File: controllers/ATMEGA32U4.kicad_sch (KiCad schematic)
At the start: 12 parts, among them J1 USB_C2, U401 ATmega32U4-A, Y401 16MHz

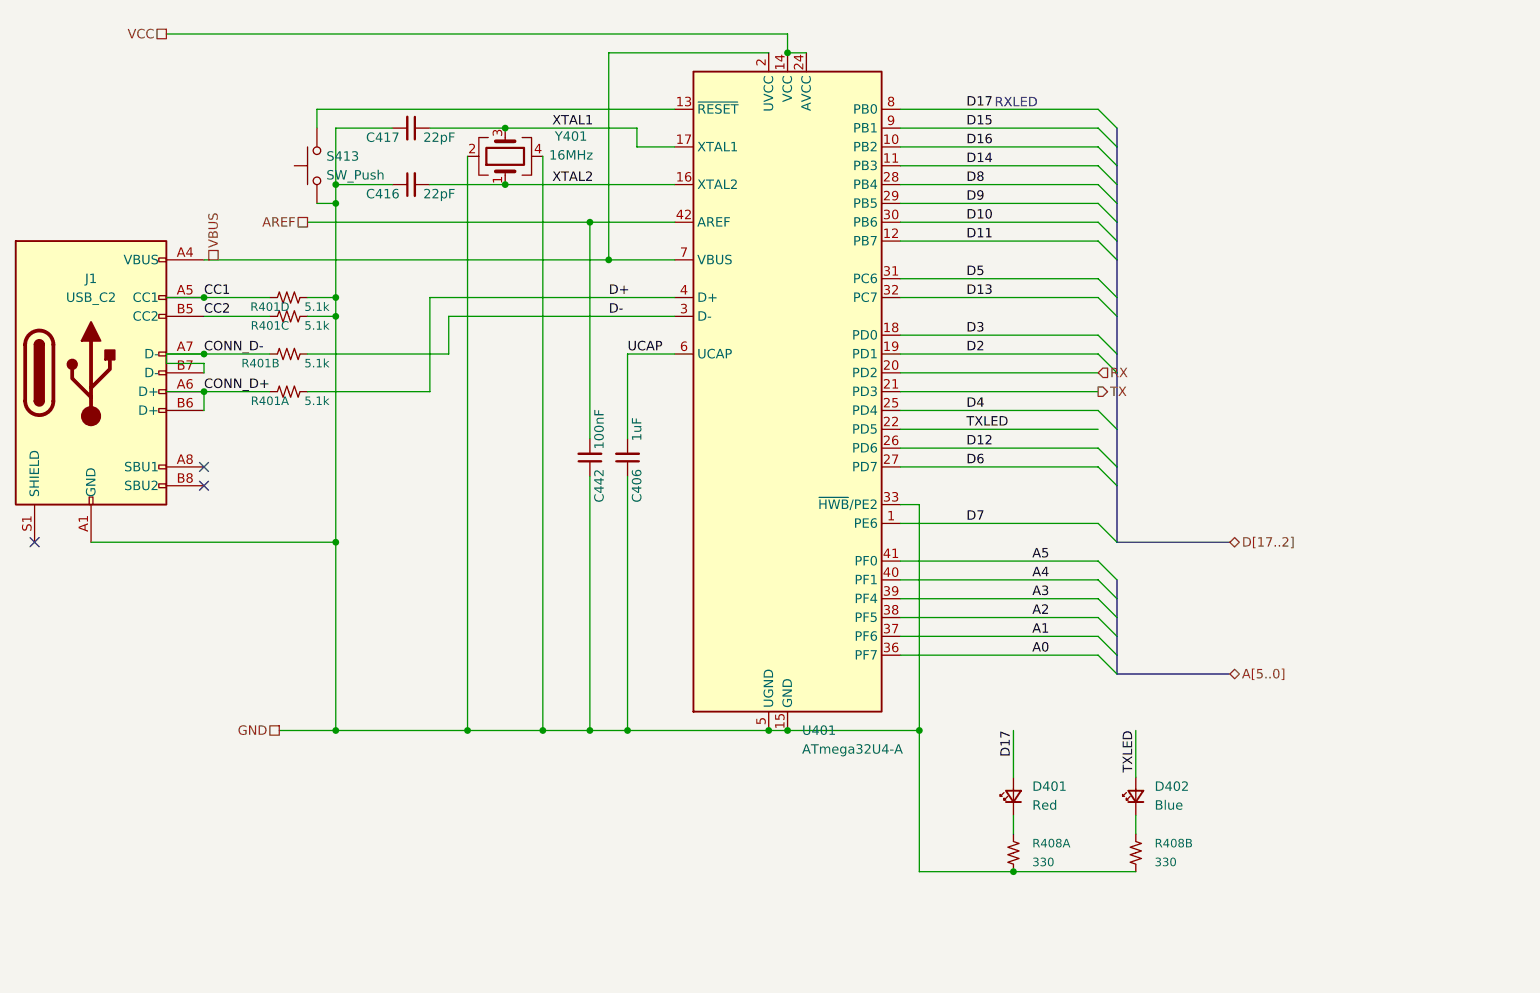
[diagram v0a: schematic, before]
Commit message: Use the separate hand sheets
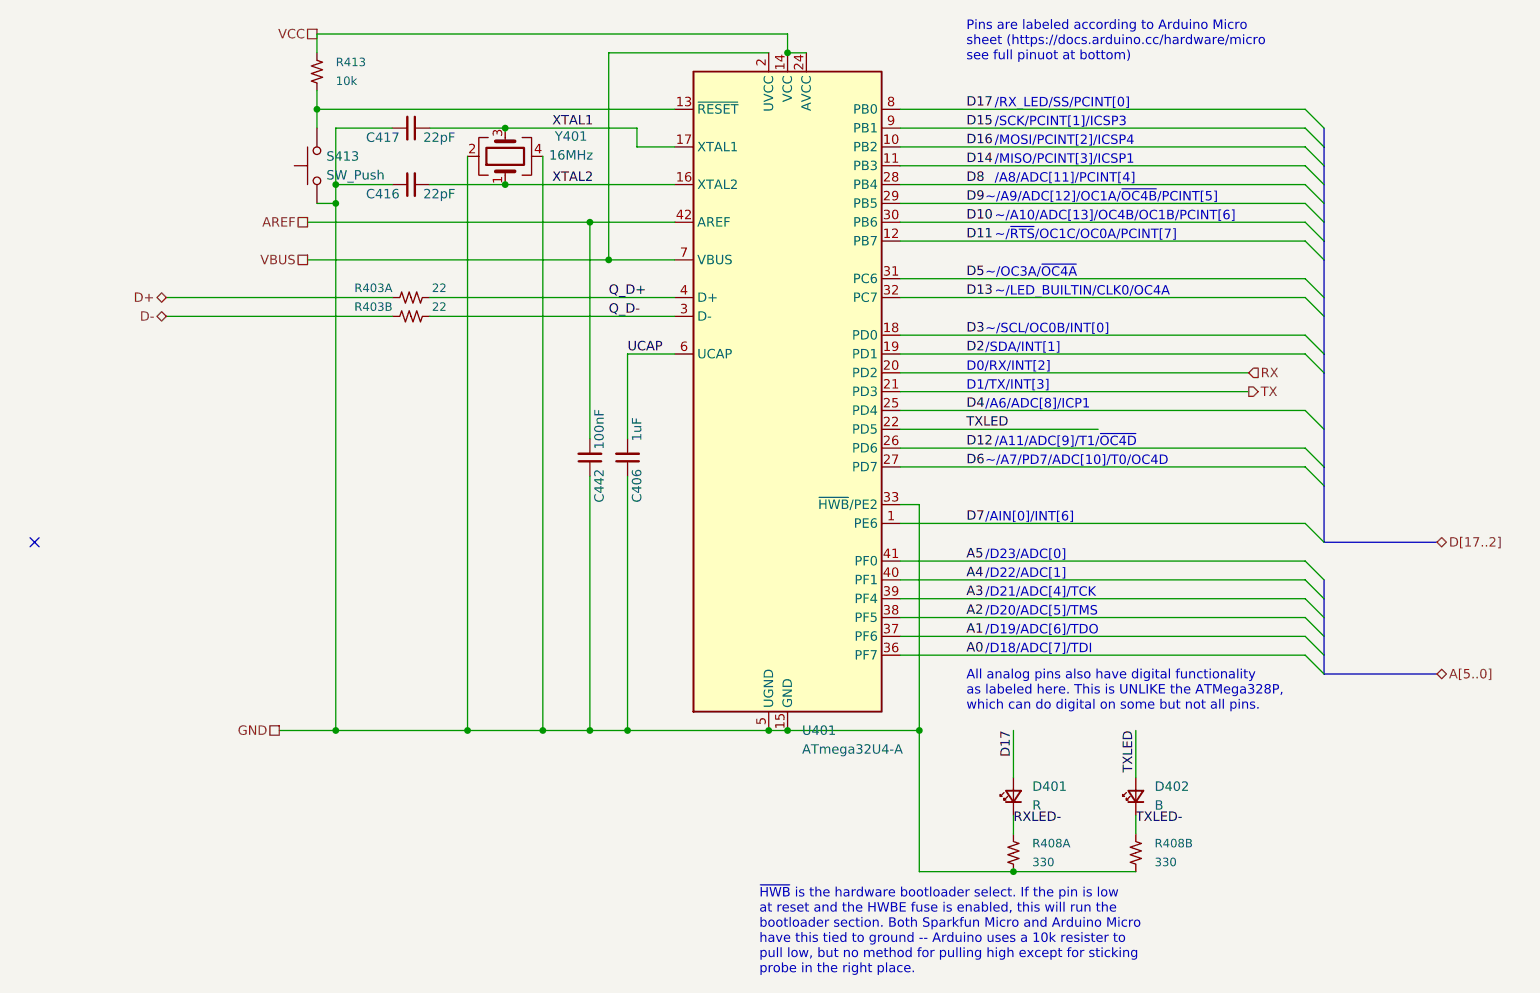
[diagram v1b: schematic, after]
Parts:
- removed J1: USB_C2, KwanSystems:USB4110, symbol Connector:USB_C_Receptacle_USB2.0
- removed R401: 5.1k, KwanSystems:R_Array_Convex_4x0402, symbol KwanSystems:RP4
- added R403: 22, KwanSystems:R_Array_Convex_2x0402, symbol KwanSystems:RP2
- added R413: 10k, Resistor_SMD:R_0402_1005Metric, symbol KwanSystems:RESISTOR
- D401: value Red -> R; Digikey (none) -> 754-1816-1-ND; Part Number (none) -> APGA1602SEC/E/KA
- D402: value Blue -> B; Digikey (none) -> 754-1434-1-ND; Part Number (none) -> APT1608QBC/D
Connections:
- net D+: now also R403.1 (4); no longer U401.4 (D+)
- net D-: now also R403.2 (4); no longer U401.3 (D-)
- net VCC: now also R413.2
- net RXLED-: now reaches D401.1 (K), R408.4 (3)
- net at S413.2, U401.13 (~{RESET}): now also R413.1
- net TXLED-: now reaches D402.1 (K), R408.3
- new net Q_D+: R403.4 (3), U401.4 (D+)
- new net Q_D-: R403.3, U401.3 (D-)
- no-connect marks 3 -> 1
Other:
- note added: "/A11/ADC[9]/T1/~{OC4D}"
- note added: "/A6/ADC[8]/ICP1"
- note added: "/A8/ADC[11]/PCINT[4]"
- note added: "/AIN[0]/INT[6]"
- note added: "/D18/ADC[7]/TDI"
- note added: "/D19/ADC[6]/TDO"
- note added: "/D20/ADC[5]/TMS"
- note added: "/D21/ADC[4]/TCK"
- note added: "/D22/ADC[1]"
- note added: "/D23/ADC[0]"
- note added: "/MISO/PCINT[3]/ICSP1"
- note added: "/MOSI/PCINT[2]/ICSP4"
- note added: "/RX_LED/SS/PCINT[0]"
- note added: "/SCK/PCINT[1]/ICSP3"
- note added: "/SDA/INT[1]"
- note added: "All analog pins also have digital functionality as labeled here. This is UNLIKE the ATMega328P, which can do digital on some but not all pins."
- note added: "D0/RX/INT[2]"
- note added: "D1/TX/INT[3]"
- note added: "Pins are labeled according to Arduino Micro sheet (https://docs.arduino.cc/hardware/micro see full pinuot at bottom)"
- note added: "~/A10/ADC[13]/OC4B/OC1B/PCINT[6]"
- note added: "~/A7/PD7/ADC[10]/T0/OC4D"
- note added: "~/A9/ADC[12]/OC1A/~{OC4B}/PCINT[5]"
- note added: "~/LED_BUILTIN/CLK0/OC4A"
- note added: "~/OC3A/~{OC4A}"
- note added: "~/SCL/OC0B/INT[0]"
- note added: "~/~{RTS}/OC1C/OC0A/PCINT[7]"
- note added: "~{HWB} is the hardware bootloader select. If the pin is low at reset and the HWBE fuse is enabled, this will run the bootloader section. Both Sparkfun Micro and Arduino Micro have this tied to ground -- Arduino uses a 10k resister to pull low, but no method for pulling high except for sticking probe in the right place."
- note removed: "RXLED"

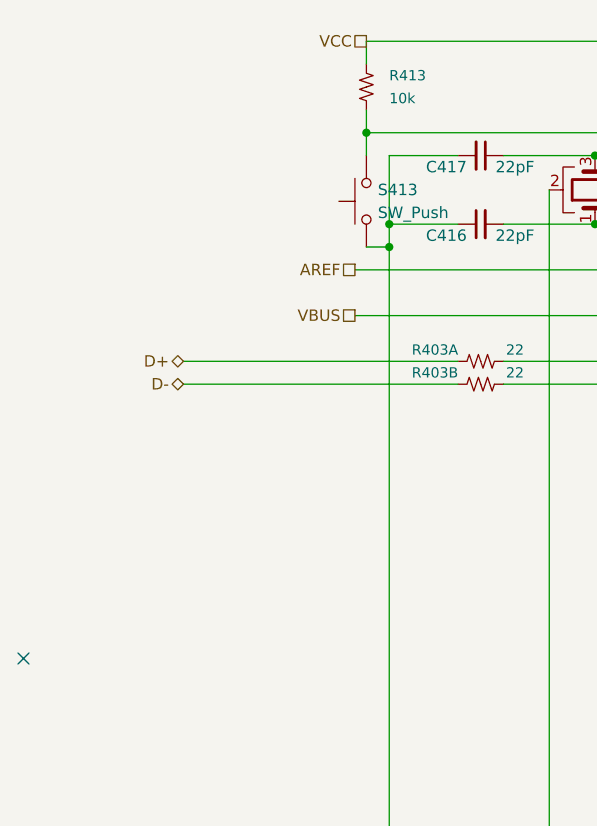
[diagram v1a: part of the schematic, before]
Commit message: Added RESET pin, updated references to LED part numbers
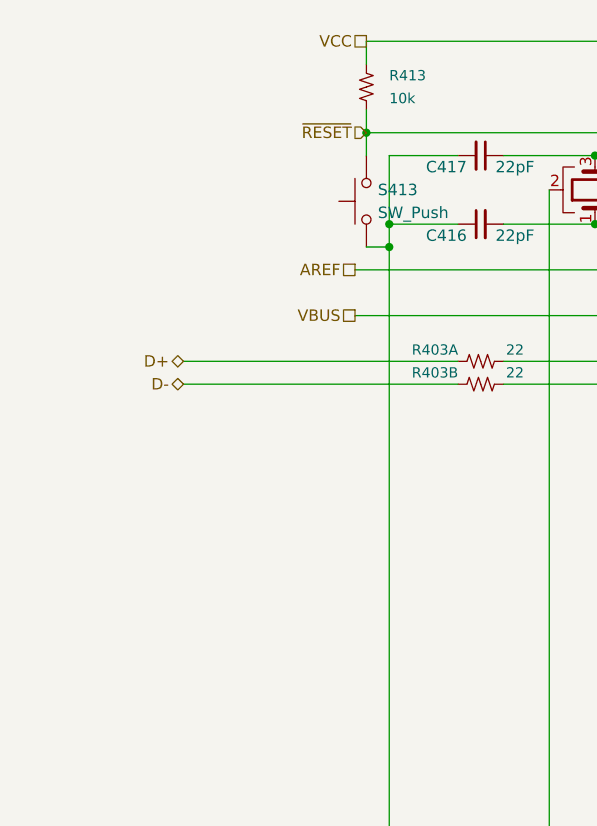
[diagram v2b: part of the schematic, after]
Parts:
- D401: Digikey 754-1816-1-ND -> 754-1123-1-ND; Part Number APGA1602SEC/E/KA -> APT1608SURCK
- D402: footprint LED_SMD:LED_0603_1608Metric -> KwanSystems:D_0603; Digikey 754-1434-1-ND -> 754-1789-1-ND; Part Number APT1608QBC/D -> APT1608VBC/D
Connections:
- net ~{RESET}: now reaches R413.1, S413.2, U401.13 (~{RESET})
- no-connect marks 1 -> 0
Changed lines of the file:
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@@
   (junction (at 57.15 69.85) (diameter 0) (color 0 0 0 0)
   )
-  (no_connect (at 16.51 115.57))
   (bus_entry (at 187.96 74.93) (size 2.54 2.54)
     (stroke (width 0) (type default))
@@
   )
   (hierarchical_label "GND" (shape passive) (at 49.53 140.97 180) (fields_autoplaced)
+    (effects (font (size 1.27 1.27)) (justify right))
+  )
+  (hierarchical_label "~{RESET}" (shape input) (at 54.61 57.15 180) (fields_autoplaced)
     (effects (font (size 1.27 1.27)) (justify right))
   )
@@
       (effects (font (size 1.27 1.27)) hide)
     )
-    (property "Digikey" "754-1816-1-ND" (at 148.59 149.86 0)
-      (effects (font (size 1.27 1.27)) hide)
-    )
-    (property "Part Number" "APGA1602SEC/E/KA" (at 148.59 149.86 0)
+    (property "Digikey" "754-1123-1-ND" (at 148.59 149.86 0)
+      (effects (font (size 1.27 1.27)) hide)
+    )
+    (property "Part Number" "APT1608SURCK" (at 148.59 149.86 0)
       (effects (font (size 1.27 1.27)) hide)
     )
@@
       (effects (font (size 1.27 1.27)) (justify right))
     )
-    (property "Footprint" "LED_SMD:LED_0603_1608Metric" (at 165.1 149.86 90)
+    (property "Footprint" "KwanSystems:D_0603" (at 165.1 149.86 90)
       (effects (font (size 1.27 1.27)) hide)
     )
@@
       (effects (font (size 1.27 1.27)) hide)
     )
-    (property "Digikey" "754-1434-1-ND" (at 165.1 149.86 0)
-      (effects (font (size 1.27 1.27)) hide)
-    )
-    (property "Part Number" "APT1608QBC/D" (at 165.1 149.86 0)
-      (effects (font (size 1.27 1.27)) hide)
-    )
+    (property "Digikey" "754-1789-1-ND" (at 165.1 149.86 0)
+      (effects (font (size 1.27 1.27)) hide)
+    )
+    (property "Part Number" "APT1608VBC/D" (at 165.1 149.86 0)
+      (effects (font (size 1.27 1.27)) hide)
+    )
